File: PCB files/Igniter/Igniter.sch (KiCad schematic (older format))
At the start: 21 parts, among them J2 Battery, J3 PT, J7 IgnitionCoil, Q1 N MOSFET, SW1 ARM

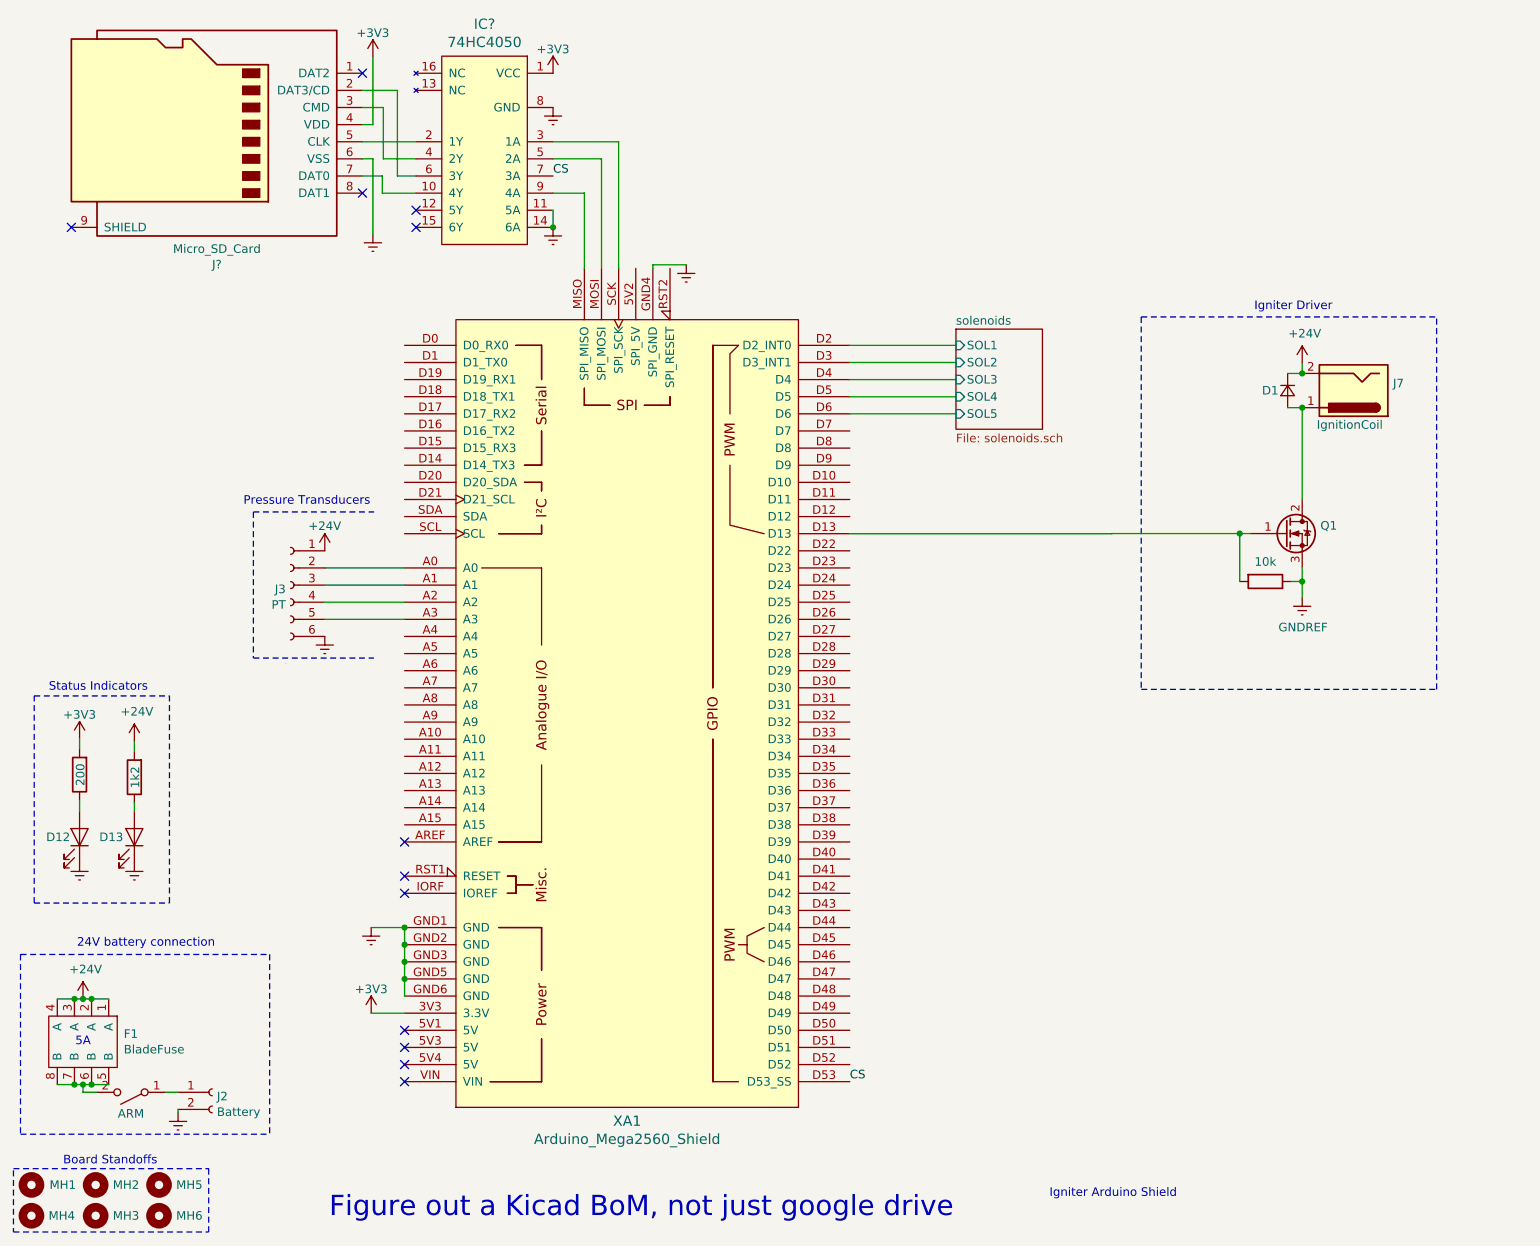
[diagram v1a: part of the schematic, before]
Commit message: 12/5/2019
-Updated netlist and board layout with added dsub15 for solenoids
-Fixed all barrel jack connectors
-Removed some 2560 pins for routing
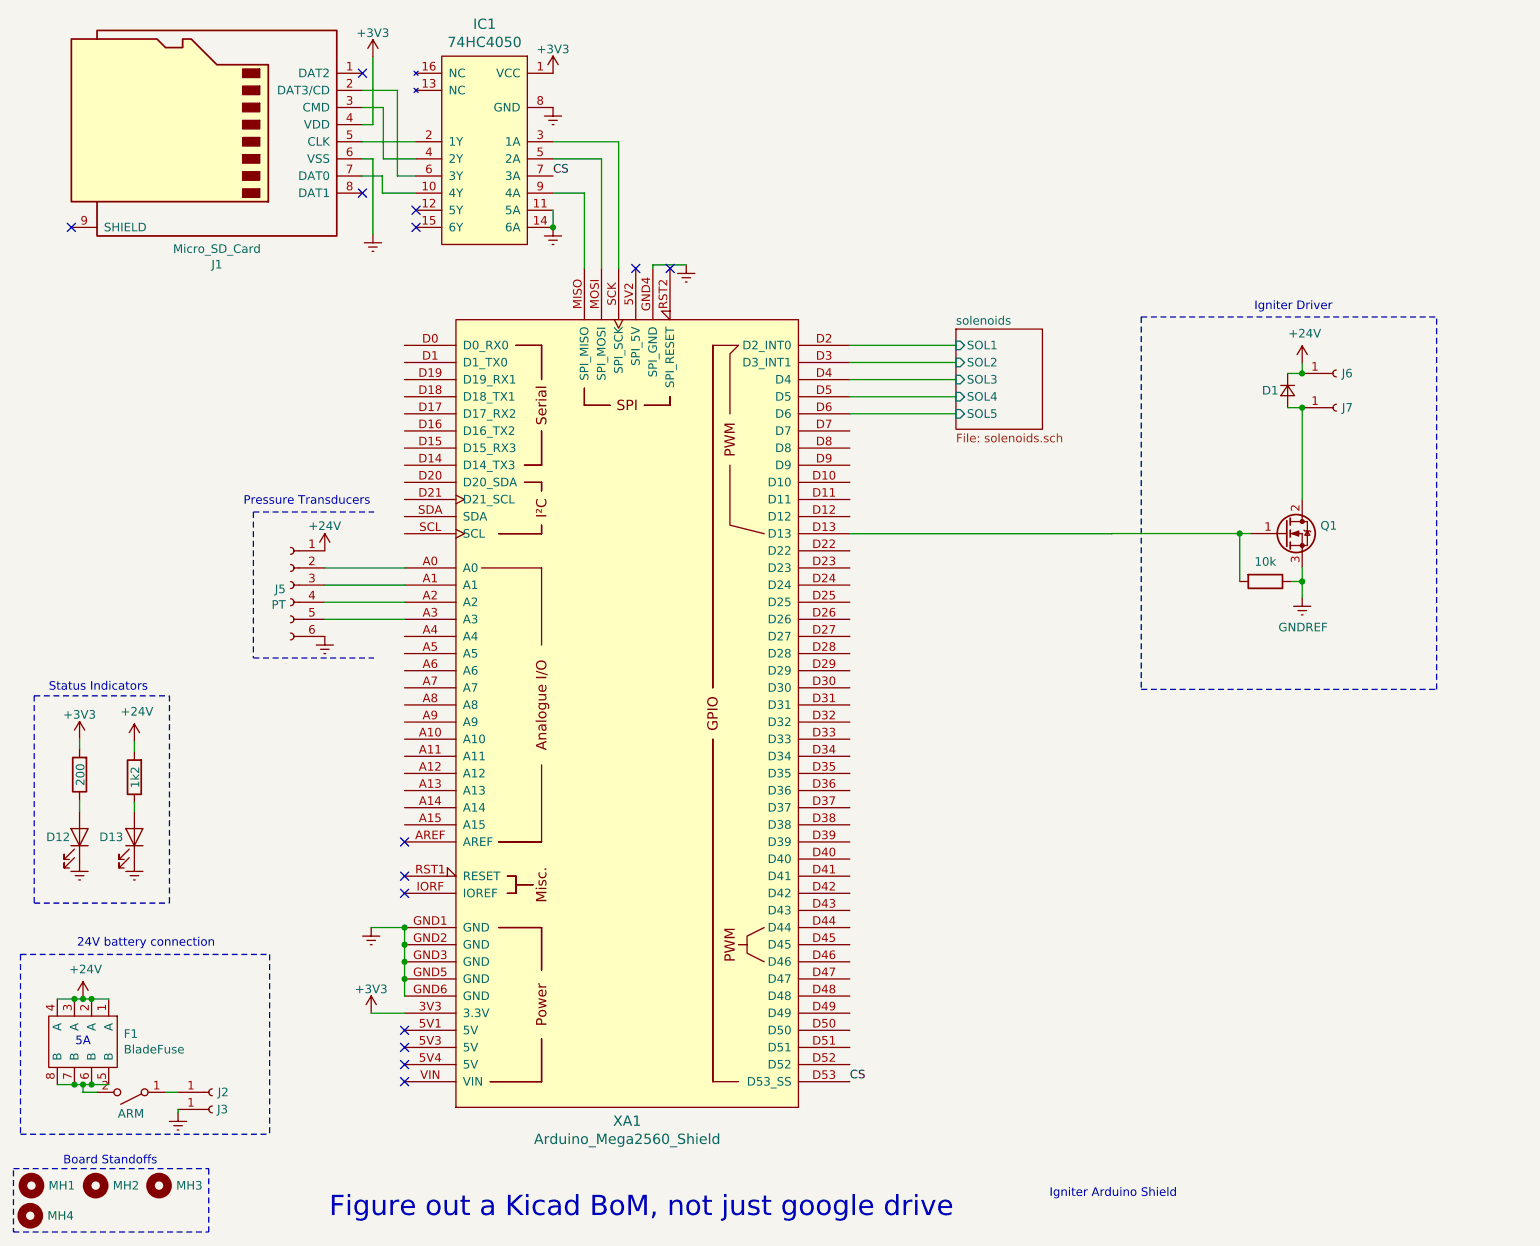
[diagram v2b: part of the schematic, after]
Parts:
- removed J2: Battery, Igniter:BananaJack15.5mm, symbol Connector:Conn_01x02_Female
- removed J7: IgnitionCoil, Igniter:BananaJack15.5mm, symbol Connector:Barrel_Jack
- removed MH1, MH2, MH5: MountingHole, MountingHole:MountingHole_2.2mm_M2, symbol Mechanical:MountingHole
- added J2: Battery +, IgniterCustom:BananaJack15.5mm, symbol Connector:Conn_01x01_Female
- added J3: Battery -, IgniterCustom:BananaJack15.5mm, symbol Connector:Conn_01x01_Female
- added J6: Ignition Coil +, IgniterCustom:BananaJack15.5mm, symbol Connector:Conn_01x01_Female
- added J7: Ignition coil -, IgniterCustom:BananaJack15.5mm, symbol Connector:Conn_01x01_Female
- added MH4: MountingHole, MountingHole:MountingHole_2.2mm_M2, symbol Mechanical:MountingHole
- SW1: footprint (none) -> Button_Switch_THT:KSA_Tactile_SPST
- XA1: footprint Arduino:Arduino_Mega2560_Shield -> Arduino:Arduino_Mega2560_Modified
- gave numbers to parts that had none: 2
- renumbered J3 to J5, MH4 to MH1, MH3 to MH2, MH6 to MH3
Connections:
- net +24V: now also J6.1 (Pin_1)
- net GNDREF: now also J3.1 (Pin_1)
- net at D1.2 (A), Q1.2 (D): now also J7.1 (Pin_1)
- net at SW1.1 (A): now also J2.1 (Pin_1)
- no-connect marks 12 -> 14
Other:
- moved on the sheet: MH1, MH2, MH3
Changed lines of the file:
@@
 LIBS:interface
 LIBS:Igniter-cache
-EELAYER 29 0
+EELAYER 26 0
 EELAYER END
 $Descr A 11000 8500
@@
 	1    0    0    -1
 $EndComp
-$Comp
-L Connector:Conn_01x02_Female J2
-U 1 1 5DAB9C23
-P 1801 7104
-F 0 "J2" H 1828 7080 50  0000 L CNN
-F 1 "Battery" H 1828 6989 50  0000 L CNN
-F 2 "Igniter:BananaJack15.5mm" H 1801 7104 50  0001 C CNN
-F 3 "~" H 1801 7104 50  0001 C CNN
-	1    1801 7104
-	1    0    0    -1
-$EndComp
 Text Notes 1011 6264 0    50   ~ 0
 24V battery connection
@@
 $Comp
 L Mechanical:MountingHole MH2
-U 1 1 5DB4BD1A
-P 1120 7645
-F 0 "MH2" H 1220 7645 50  0000 L CNN
-F 1 "MountingHole" H 1220 7600 50  0001 L CNN
-F 2 "MountingHole:MountingHole_2.2mm_M2" H 1120 7645 50  0001 C CNN
-F 3 "~" H 1120 7645 50  0001 C CNN
-	1    1120 7645
+U 1 1 5DB4BE36
+P 1120 7649
+F 0 "MH2" H 1220 7649 50  0000 L CNN
+F 1 "MountingHole" H 1220 7604 50  0001 L CNN
+F 2 "MountingHole:MountingHole_2.2mm_M2" H 1120 7649 50  0001 C CNN
+F 3 "~" H 1120 7649 50  0001 C CNN
+	1    1120 7649
 	1    0    0    -1
 $EndComp
 $Comp
-L Mechanical:MountingHole MH3
-U 1 1 5DB4BE36
-P 1120 7825
-F 0 "MH3" H 1220 7825 50  0000 L CNN
-F 1 "MountingHole" H 1220 7780 50  0001 L CNN
-F 2 "MountingHole:MountingHole_2.2mm_M2" H 1120 7825 50  0001 C CNN
-F 3 "~" H 1120 7825 50  0001 C CNN
-	1    1120 7825
-	1    0    0    -1
-$EndComp
-$Comp
-L Mechanical:MountingHole MH4
+L Mechanical:MountingHole MH1
 U 1 1 5DB4BEEA
-P 745 7825
-F 0 "MH4" H 645 7825 50  0000 R CNN
-F 1 "MountingHole" H 845 7780 50  0001 L CNN
-F 2 "MountingHole:MountingHole_2.2mm_M2" H 745 7825 50  0001 C CNN
-F 3 "~" H 745 7825 50  0001 C CNN
-	1    745  7825
+P 745 7649
+F 0 "MH1" H 645 7649 50  0000 R CNN
+F 1 "MountingHole" H 845 7604 50  0001 L CNN
+F 2 "MountingHole:MountingHole_2.2mm_M2" H 745 7649 50  0001 C CNN
+F 3 "~" H 745 7649 50  0001 C CNN
+	1    745  7649
 	-1   0    0    1
-$EndComp
-$Comp
-L Mechanical:MountingHole MH1
-U 1 1 5DB4BFCA
-P 745 7645
-F 0 "MH1" V 745 7385 50  0000 L CNN
-F 1 "MountingHole" H 845 7600 50  0001 L CNN
-F 2 "MountingHole:MountingHole_2.2mm_M2" H 745 7645 50  0001 C CNN
-F 3 "~" H 745 7645 50  0001 C CNN
-	1    745  7645
-	0    -1   -1   0
 $EndComp
 Wire Wire Line
@@
 F 0 "SW1" H 1326 6879 50  0001 C CNN
 F 1 "ARM" H 1326 7229 50  0000 C CNN
-F 2 "" H 1326 7104 50  0001 C CNN
+F 2 "Button_Switch_THT:KSA_Tactile_SPST" H 1326 7104 50  0001 C CNN
 F 3 "~" H 1326 7104 50  0001 C CNN
 	1    1326 7104
@@
 	640  7560 640  7920
 $Comp
-L Mechanical:MountingHole MH5
-U 1 1 5DCE1DB8
-P 1490 7645
-F 0 "MH5" H 1590 7645 50  0000 L CNN
-F 1 "MountingHole" H 1590 7600 50  0001 L CNN
-F 2 "MountingHole:MountingHole_2.2mm_M2" H 1490 7645 50  0001 C CNN
-F 3 "~" H 1490 7645 50  0001 C CNN
-	1    1490 7645
-	1    0    0    -1
-$EndComp
-$Comp
-L Mechanical:MountingHole MH6
+L Mechanical:MountingHole MH3
 U 1 1 5DCE1DBE
-P 1490 7825
-F 0 "MH6" H 1590 7825 50  0000 L CNN
-F 1 "MountingHole" H 1590 7780 50  0001 L CNN
-F 2 "MountingHole:MountingHole_2.2mm_M2" H 1490 7825 50  0001 C CNN
-F 3 "~" H 1490 7825 50  0001 C CNN
-	1    1490 7825
+P 1490 7649
+F 0 "MH3" H 1590 7649 50  0000 L CNN
+F 1 "MountingHole" H 1590 7604 50  0001 L CNN
+F 2 "MountingHole:MountingHole_2.2mm_M2" H 1490 7649 50  0001 C CNN
+F 3 "~" H 1490 7649 50  0001 C CNN
+	1    1490 7649
 	1    0    0    -1
 $EndComp
@@
 $EndComp
 $Comp
-L Connector:Conn_01x06_Female J3
+L Connector:Conn_01x06_Female J5
 U 1 1 5DEB9566
 P 2258 4142
-F 0 "J3" H 2286 4118 50  0000 L CNN
+F 0 "J5" H 2286 4118 50  0000 L CNN
 F 1 "PT" H 2286 4027 50  0000 L CNN
 F 2 "Connector_Dsub:DSUB-9_Male_Horizontal_P2.77x2.54mm_EdgePinOffset9.40mm" H 2258 4142 50  0001 C CNN
@@
 F 0 "XA1" H 4224 2512 60  0000 C CNN
 F 1 "Arduino_Mega2560_Shield" H 4224 2406 60  0000 C CNN
-F 2 "Arduino:Arduino_Mega2560_Shield" H 4924 7642 60  0001 C CNN
+F 2 "Arduino:Arduino_Mega2560_Modified" H 4924 7642 60  0001 C CNN
 F 3 "https://store.arduino.cc/arduino-mega-2560-rev3" H 4924 7642 60  0001 C CNN
 	1    4224 4892
 	1    0    0    -1
 $EndComp
-Connection ~ 8166 3106
 Wire Wire Line
 	8081 3106 8166 3106
-Connection ~ 8166 2906
-Wire Wire Line
-	8081 2906 8166 2906
+Wire Wire Line
+	8081 2906 8165 2906
 $Comp
 L Device:D_Small D1
@@
 	1    0    0    -1
 $EndComp
-$Comp
-L Connector:Barrel_Jack J7
-U 1 1 5DAB74DD
-P 8466 3006
-AR Path="/5DAB74DD" Ref="J7"  Part="1"
-AR Path="/5D9BEB88/5DAB74DD" Ref="J?"  Part="1"
-F 0 "J7" H 8236 2964 50  0000 R CNN
-F 1 "IgnitionCoil" H 8681 3206 50  0000 R CNN
-F 2 "Igniter:BananaJack15.5mm" H 8516 2966 50  0001 C CNN
-F 3 "~" H 8516 2966 50  0001 C CNN
-	1    8466 3006
-	-1   0    0    1
-$EndComp
 NoConn ~ 2924 5842
 NoConn ~ 2924 5942
@@
 P 1778 1453
 AR Path="/5DC64D13/5DF09A80" Ref="J?"  Part="1"
-AR Path="/5DF09A80" Ref="J?"  Part="1"
-F 0 "J?" H 1728 636 50  0000 C CNN
+AR Path="/5DF09A80" Ref="J1"  Part="1"
+F 0 "J1" H 1728 636 50  0000 C CNN
 F 1 "Micro_SD_Card" H 1728 727 50  0000 C CNN
 F 2 "Connector_Card:microSD_HC_Hirose_DM3BT-DSF-PEJS" H 2928 1753 50  0001 C CNN
@@
 $EndComp
 $Comp
-L power:GNDREF #PWR?
+L power:GNDREF #PWR06
 U 1 1 5DF09A7A
 P 2739 2093
-AR Path="/5DF09A7A" Ref="#PWR?"  Part="1"
+AR Path="/5DF09A7A" Ref="#PWR06"  Part="1"
 AR Path="/5DC64D13/5DF09A7A" Ref="#PWR?"  Part="1"
-F 0 "#PWR?" H 2739 1843 50  0001 C CNN
+F 0 "#PWR06" H 2739 1843 50  0001 C CNN
 F 1 "GNDREF" H 2744 1920 50  0001 C CNN
 F 2 "" H 2739 2093 50  0001 C CNN
@@
 $EndComp
 $Comp
-L power:+3V3 #PWR?
+L power:+3V3 #PWR05
 U 1 1 5DF09A62
 P 2739 1058
-AR Path="/5DF09A62" Ref="#PWR?"  Part="1"
+AR Path="/5DF09A62" Ref="#PWR05"  Part="1"
 AR Path="/5DC64D13/5DF09A62" Ref="#PWR?"  Part="1"
-F 0 "#PWR?" H 2739 908 50  0001 C CNN
+F 0 "#PWR05" H 2739 908 50  0001 C CNN
 F 1 "+3V3" H 2739 1198 50  0000 C CNN
 F 2 "" H 2739 1058 50  0001 C CNN
@@
 P 3391 1603
 AR Path="/5DC64D13/5DF09A68" Ref="IC?"  Part="1"
-AR Path="/5DF09A68" Ref="IC?"  Part="1"
-F 0 "IC?" H 3391 2340 60  0000 C CNN
+AR Path="/5DF09A68" Ref="IC1"  Part="1"
+F 0 "IC1" H 3391 2340 60  0000 C CNN
 F 1 "74HC4050" H 3391 2234 60  0000 C CNN
 F 2 "Package_SO:SOP-16_4.4x10.4mm_P1.27mm" H 3291 1603 60  0001 C CNN
@@
 $EndComp
 $Comp
-L power:+3V3 #PWR?
+L power:+3V3 #PWR09
 U 1 1 5DF09A74
 P 3791 1153
-F 0 "#PWR?" H 3791 1003 50  0001 C CNN
+F 0 "#PWR09" H 3791 1003 50  0001 C CNN
 F 1 "+3V3" H 3791 1293 50  0000 C CNN
 F 2 "" H 3791 1153 50  0001 C CNN
@@
 NoConn ~ 2991 1953
 $Comp
-L power:GNDREF #PWR?
+L power:GNDREF #PWR013
 U 1 1 5DF09A89
 P 3791 2053
-AR Path="/5DF09A89" Ref="#PWR?"  Part="1"
+AR Path="/5DF09A89" Ref="#PWR013"  Part="1"
 AR Path="/5DC64D13/5DF09A89" Ref="#PWR?"  Part="1"
-F 0 "#PWR?" H 3791 1803 50  0001 C CNN
+F 0 "#PWR013" H 3791 1803 50  0001 C CNN
 F 1 "GNDREF" H 3796 1880 50  0001 C CNN
 F 2 "" H 3791 2053 50  0001 C CNN
@@
 	2991 1753 2882 1753
 $Comp
-L power:GNDREF #PWR?
+L power:GNDREF #PWR010
 U 1 1 5DF09A6E
 P 3791 1353
-F 0 "#PWR?" H 3791 1103 50  0001 C CNN
+F 0 "#PWR010" H 3791 1103 50  0001 C CNN
 F 1 "GNDREF" H 3796 1180 50  0001 C CNN
 F 2 "" H 3791 1353 50  0001 C CNN
@@
 Wire Wire Line
 	4174 1553 4174 2292
+$Comp
+L Connector:Conn_01x01_Female J2
+U 1 1 5DEA7B33
+P 1801 7104
+F 0 "J2" H 1833 7104 50  0000 L CNN
+F 1 "Battery +" H 1828 7039 50  0001 L CNN
+F 2 "IgniterCustom:BananaJack15.5mm" H 1801 7104 50  0001 C CNN
+F 3 "~" H 1801 7104 50  0001 C CNN
+	1    1801 7104
+	1    0    0    -1
+$EndComp
+$Comp
+L Connector:Conn_01x01_Female J3
+U 1 1 5DEA7B7D
+P 1801 7204
+F 0 "J3" H 1829 7204 50  0000 L CNN
+F 1 "Battery -" H 1828 7139 50  0001 L CNN
+F 2 "IgniterCustom:BananaJack15.5mm" H 1801 7204 50  0001 C CNN
+F 3 "~" H 1801 7204 50  0001 C CNN
+	1    1801 7204
+	1    0    0    -1
+$EndComp
+$Comp
+L Connector:Conn_01x01_Female J6
+U 1 1 5DEA8937
+P 8365 2906
+F 0 "J6" H 8397 2906 50  0000 L CNN
+F 1 "Ignition Coil +" H 8392 2841 50  0001 L CNN
+F 2 "IgniterCustom:BananaJack15.5mm" H 8365 2906 50  0001 C CNN
+F 3 "~" H 8365 2906 50  0001 C CNN
+	1    8365 2906
+	1    0    0    -1
+$EndComp
+Connection ~ 8165 2906
+Wire Wire Line
+	8165 2906 8166 2906
+$Comp
+L Connector:Conn_01x01_Female J7
+U 1 1 5DEA8AF3
+P 8366 3106
+F 0 "J7" H 8398 3106 50  0000 L CNN
+F 1 "Ignition coil -" H 8393 3041 50  0001 L CNN
+F 2 "IgniterCustom:BananaJack15.5mm" H 8366 3106 50  0001 C CNN
+F 3 "~" H 8366 3106 50  0001 C CNN
+	1    8366 3106
+	1    0    0    -1
+$EndComp
+Connection ~ 8166 3106
+$Comp
+L Mechanical:MountingHole MH4
+U 1 1 5DEB0FB5
+P 738 7825
+F 0 "MH4" H 838 7825 50  0000 L CNN
+F 1 "MountingHole" H 838 7780 50  0001 L CNN
+F 2 "MountingHole:MountingHole_2.2mm_M2" H 738 7825 50  0001 C CNN
+F 3 "~" H 738 7825 50  0001 C CNN
+	1    738  7825
+	1    0    0    -1
+$EndComp
+NoConn ~ 4274 2293
+NoConn ~ 4475 2293
 $EndSCHEMATC
